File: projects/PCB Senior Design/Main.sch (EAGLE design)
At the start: 117 parts, among them IC1 74LVC2G34DBVR, J8 U.FL, J9 NANO_SIM, Q1 BSS138, Q2 2.5A/30V/105mΩ, U1 UBLOX_SAM_M8Q-0-10, U10 TCA9406DCU, U11 TXB0104, U13 LP2985-33DBVR, U2 32KB NRF51822, U3 MIC5225-3.3, U4 NCP1117ST50T3G, U6 SARA-R410M-2B, U7 MCP73831, U8 AP7361C-33FGE, U9 AP2112K-3.3, X1 POWERSUPPLY_DC21MMX, Y1 32.768kHz (535-9166-2-ND), Y2 CSTCE16M0V53-R0 16MHZ

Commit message: Made some connections
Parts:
- removed B2: ARDUINO_UNO_R3_SHIELDNOLABELS, SparkFun-Boards:ARDUINO_UNO_R3_SHIELDNOLABELS
- removed D9: PRTR5V0U2F, ublox:PRTR5V0U2F
- removed J15: (no value), SparkFun-Connectors:6_PIN_SERIAL_TARGETNO_SILK
- removed JP10: IOREF-SEL, SparkFun-Jumpers:JUMPER-SMT_3_NO_SILK
- removed JP6, JP9: JUMPER-SMT_2_NC_TRACE_SILK, SparkFun-Jumpers:JUMPER-SMT_2_NC_TRACE_SILK
- removed S3: PWR_ON, SparkFun-Switches:MOMENTARY-SWITCH-SPST-SMD-5.2-REDUNDANT
- removed S4: RESET, SparkFun-Switches:MOMENTARY-SWITCH-SPST-SMD-5.2-REDUNDANT
- removed S6: (no value), SparkFun-Switches:SWITCH-DPDT-SMD-AYZ0202
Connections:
- removed net +3V3: C33.2, U13.OUT
- removed net HARDRX-ARDUINO: B2.RX, S6.1
- removed net HARDTX-ARDUINO: B2.TX, S6.4
- removed net IOREF: B2.IOREF, C25.1, J15.VCC, JP10.2, U10.VCCB, U11.VCCB
- removed net N$10: B2.*D6, JP6.1
- removed net N$11: D9.1, J12.D-
- removed net N$13: D9.3, J12.D+
- removed net N$6: B2.*D5, JP9.1
- removed net RX-ARDUINO: J15.RXI, S6.2, U11.B2
- removed net SOFTRX-ARDUINO: B2.D8, S6.3
- removed net SOFTTX-ARDUINO: B2.*D9, S6.6
- removed net TX-ARDUINO: J15.TXO, S6.5, U11.B3
- new net RX-ARD: U11.B2, ZU4.(ICP)PB0
- new net TX-ARD: U11.B3, ZU4.(OC1)PB1
- net ARDUINO-3.3V: now also C33.2, U13.OUT; no longer B2.3.3V, JP10.3
- net ARDUINO-5V: now also C25.1, U10.VCCB, U11.VCCB; no longer B2.5V, JP10.1
- net D+: no longer D9.4
- net D-: no longer D9.6
- net GND: no longer B2.GND@0, B2.GND@1, B2.GND@2, D9.2, J15.GND, S3.1, S4.1
- net PWR_ON: now also ZU4.(T1)PD5; no longer JP9.2, S3.2
- net RESET_N: now also ZU4.(AIN0)PD6; no longer JP6.2, S4.2
- net V_USB: no longer D9.5
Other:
- note removed: "6-Pin Serial Port"
- note removed: "Arduino Pins"
- note removed: "Hardware Serial Port (D0 = RX, D1 = TX)"
- note removed: "If the Arduino does not supply IOREF, Use JP1 to set it to either 5V or 3.3V."
- note removed: "JP2 and JP3 can disconnect control lines from Arduino."
- note removed: "Software serial port (D8 = RX, D9 = TX)"
- note removed: "UART-Slect"
- moved on the sheet: C24, C25

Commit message: More cleaning up, serial to ATMega pt 1
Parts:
- removed C33: 1u, SmartPrj:C-EU0603-RND
- removed D7: Yellow, SparkFun-LED:LED-YELLOW0603
- removed D8: RED, SparkFun-LED:LED-RED0603
- removed FRAME3: FRAME-LETTER, SparkFun-Aesthetics:FRAME-LETTER
- removed J12: (no value), SparkFun-Connectors:USB_MICRO-B_HALF_PTH_MILL
- removed J13: (no value), SparkFun-Connectors:QWIIC_CONNECTORJS-1MM
- removed J14: (no value), SparkFun-Connectors:JST_2MM_MALESMD
- removed J16: (no value), SparkFun-Connectors:CONN_01PTH_NO_SILK_YES_STOP
- removed J17, J18: (no value), SparkFun-Connectors:CONN_021X02_NO_SILK
- removed J6, J7: (no value), SparkFun-Connectors:CONN_031X03_NO_SILK
- removed JP4, JP5: JUMPER-SMT_2_NC_TRACE_SILK, SparkFun-Jumpers:JUMPER-SMT_2_NC_TRACE_SILK
- removed PC1, PC2: 47u, rcl:CPOL-EUD
- removed R10: 1k, SparkFun-Resistors:1KOHM-0603-1/10W-1%
- removed R12: 1M, SmartPrj:R-EU_R0603
- removed R9: 2.0k, SparkFun-Resistors:2.0KOHM-0603-1/10W-5%
- removed S5: (no value), SparkFun-Switches:SWITCH-DPDT-SMD-AYZ0202
- removed TP_XT2: TP_SP, SmartPrj:TP_SP
- removed U10: TCA9406DCU, ublox:TCA9406DCU
- removed U11: TXB0104, SparkFun-IC-Comms:TXB0104PWR
- removed U13: LP2985-33DBVR, SmartPrj:LP2985-XXDBVR33
- removed X1: POWERSUPPLY_DC21MMX, SmartPrj:POWERSUPPLY_DC21MMX
- removed Y2: CSTCE16M0V53-R0 16MHZ, SmartPrj:RESONATORMU
- added C28: 22p, SmartPrj:C-EU0603-RND
- added C7: 4.7uF, SparkFun-Capacitors:4.7UF-0603-6.3V-(10%)
- added D12: RED, SparkFun-LED:LED-RED0603
- added D9: Yellow, SparkFun-LED:LED-YELLOW0603
- added F1: MF-MSMF050-2 500mA, rcl:L-EUL1812
- added J1: (no value), SparkFun-Connectors:USB_MICRO-B_HALF_PTH_MILL
- added J2: (no value), SparkFun-Connectors:JST_2MM_MALESMD
- added L3: BLM21, wuerth-elektronik:WE-CBF_0805
- added Q3: 2.5A/30V/105mΩ, SparkFun-DiscreteSemi:MOSFET_PCH-DMG2307L
- added Q4: 8MHz, special:XTAL
- added R15: 1k, SparkFun-Resistors:1KOHM-0603-1/10W-1%
- added RN2: 1K, resistor-dil:4R-NCAY16
- added RN3: 10K, resistor-dil:4R-NCAY16
- added RN4: 22R, resistor-dil:4R-NCAY16
- added U5: MCP73831, SparkFun-PowerIC:MCP73831
- added Z1, Z2: CG0603MLC-05E, varistor:VARISTORCN0603
- C21: value 4.7uF -> 0.1uF; device SparkFun-Capacitors:4.7UF-0603-6.3V-(10%) -> SparkFun-Capacitors:0.1UF-0603-25V-(+80/-20%)
- C22, C23: value 4.7uF -> 100n; device SparkFun-Capacitors:4.7UF-0603-6.3V-(10%) -> SmartPrj:C-EU0603-RND
- C24: value 0.1uF -> 1u; device SparkFun-Capacitors:0.1UF-0603-25V-(+80/-20%) -> SmartPrj:C-EU0603-RND
- C25: value 0.1uF -> 22p; device SparkFun-Capacitors:0.1UF-0603-25V-(+80/-20%) -> SmartPrj:C-EU0603-RND
- C26, C27: value 1.0uF -> 4.7uF; device SparkFun-Capacitors:1.0UF-0603-16V-10% -> SparkFun-Capacitors:4.7UF-0603-6.3V-(10%)
- C6: value 100n -> 0.1uF; device SmartPrj:C-EU0603-RND -> SparkFun-Capacitors:0.1UF-0603-25V-(+80/-20%)
- D1: value M7 -> 1A/23V/620mV; device diode:DIODE-SMB -> SparkFun-DiscreteSemi:DIODE-SCHOTTKY-BAT20J
- D5: value 1A/23V/620mV -> CD1206-S01575; device SparkFun-DiscreteSemi:DIODE-SCHOTTKY-BAT20J -> diode:DIODE-MINIMELF
- Q2: value 2.5A/30V/105mΩ -> 8MHz; device SparkFun-DiscreteSemi:MOSFET_PCH-DMG2307L -> special:XTAL
- R1: value 470 -> 10k; device SparkFun-Resistors:470OHM-0603-1/10W-1% -> SparkFun-Resistors:10KOHM-0603-1/10W-1%
- R11: value 47k -> 2.0k; device SparkFun-Resistors:47KOHM-0603-1/10W-1% -> SparkFun-Resistors:2.0KOHM-0603-1/10W-5%
- R2: value 470 -> 1k; device SparkFun-Resistors:470OHM-0603-1/10W-1% -> SparkFun-Resistors:1KOHM-0603-1/10W-1%
- R6: value 10k -> 1M; device SparkFun-Resistors:10KOHM-0603-1/10W-1% -> SmartPrj:R-EU_R0603
- R7: value 1k -> 1M; device SparkFun-Resistors:1KOHM-0603-1/10W-1% -> SmartPrj:R-EU_R0603
- U4: value NCP1117ST50T3G -> TCA9406DCU; device linear:MC33269ST-3.3T3 -> ublox:TCA9406DCU
- U7: value MCP73831 -> TXB0104; device SparkFun-PowerIC:MCP73831 -> SparkFun-IC-Comms:TXB0104PWR
- U8: value AP7361C-33FGE -> ATMEGA16U2-MU(R); device ublox:AP7361C-33FGE -> SmartPrj:ATMEGA16U2-MU
- U9: value AP2112K-3.3 -> AP7361C-33FGE; device SparkFun-IC-Power:V_REG_AP2112K-3.3V -> ublox:AP7361C-33FGE
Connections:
- net ANT_DET renamed N$2
- removed net !RESET: U1.!RST
- removed net !SAFE: U1.!SAFEBOOT
- removed net AD4/SDA: ZU4.(ADC4)PC4
- removed net AD5/SCL: ZU4.(ADC5)PC5
- removed net ARDUINO-3.3V: C33.2, U13.OUT
- removed net ARDUINO-5V: C25.1, S5.2, S5.5, U10.VCCB, U11.VCCB
- removed net CTS: J7.3, U6.CTS
- removed net DCD: J6.2, U6.DCD
- removed net DSR: J6.1, U6.DSR
- removed net GPIO2: R11.2, U6.GPIO2, U9.EN
- removed net GPIO3-CELL: U11.A1, U6.GPIO3
- removed net GPIO3-QWIIC: J16.1, U11.B1
- removed net GPS-3.3V: C27.1, J13.2, U9.OUT
- removed net INT: U1.INT
- removed net N$2 (its old number): D7.C, R7.2
- removed net N$3: R7.1, U7.STAT
- removed net N$4: R9.2, U7.PROG
- removed net N$5: D8.A, R10.1
- removed net NETWORK_LED: U6.GPIO1
- removed net PPS: U1.TPULSE
- removed net PWRIN: D1.A, X1.2
- removed net RI: J7.1, U6.RI
- removed net RTS: J6.3, JP4.2, U6.RTS
- removed net RXI: R2.2
- removed net RXLV: R2.1, U1.RX
- removed net SCL: R14.2, R3.1
- removed net SCL-QWIIC: J13.4, J17.2, U10.SCL_B
- removed net SDA: R13.2, R4.1
- removed net SDA-QWIIC: J13.3, J17.1, U10.SDA_B
- removed net TXLV: R1.1, U1.TX
- removed net TXO: R1.2
- removed net VUSB_DET: U6.VUSB_DET
- new net GPIO3-CELL1: U7.A1
- new net GPIO3-QWIIC1: U7.B1
- new net M8RXD: U8.(TXD1/INT3)PD3
- new net M8TXD: U8.(RXD1/AIN1/INT2)PD2
- new net N$1: D9.C, R2.2
- new net N$10: R11.2, U5.PROG
- new net N$11: D12.A, R15.1
- new net N$6: R2.1, U5.STAT
- new net RD+: RN4D.1, U8.D+
- new net RD-: RN4A.1, U8.D-
- new net RESET1: C23.2
- new net RESET2: D5.A, RN3C.2, U8.RESET(PC1/DW)
- new net SCL-GPS: R14.2, R3.1, U4.SCL_B
- new net SDA-GPS: R13.2, R4.1, U4.SDA_B
- new net TP_VUCAP: C24.1, U8.UCAP
- new net USBVCC: F1.1, U8.UVCC
- new net XT1: C25.1, Q4.1, R6.1, U8.XTAL1
- new net XT2: C28.1, Q4.2, R6.2, U8.XTAL2(PC0)
- net +5V: now also C22.1, D5.C, RN3C.1, U8.AVCC, U8.VCC; no longer C31.2, C6.2, D3.C, ICSP.2, L4.1, PC2.+, RN1D.2, U13.IN, U13.ON/!OFF, U4.OUT, U4.OUT@1, ZU4.VCC
- net 1.8V: now also C6.1, U4.OE, U4.VCCA, U7.OE, U7.VCCA; no longer C24.1, U10.OE, U10.VCCA, U11.OE, U11.VCCA
- net 3.3V: now also C21.1, C27.1, C31.2, D3.C, ICSP.2, L4.1, R15.2, RN1D.2, U4.VCCB, U7.VCCB, U9.OUT, ZU4.VCC; no longer C23.1, C26.1, R10.2, U8.OUT, U9.IN
- net D+: now also J1.D+, RN4D.2, Z1.1; no longer U6.USB_D+
- net D-: now also J1.D-, RN4A.2, Z2.1; no longer U6.USB_D-
- net DTR: now also C23.1, RN2D.1, U8.(CTS/HWB/AIN6/TO/INT7)PD7; no longer J7.2, JP5.2, U6.DTR
- net GND: now also C28.2, C6.2, C7.2, D12.C, J1.GND, J2.-, L3.1, R1.1, RN2D.2, U4.GND, U5.VSS, U6.DTR, U6.RTS, U7.GND, U8.PAD, U8.UGND; no longer C23.2, C33.1, C6.1, D8.C, J12.GND, J13.1, J14.-, J18.1, JP4.1, JP5.1, PC1.-, PC2.-, R6.1, R9.1, U10.GND, U11.GND, U13.GND, U4.GND/ADJ, U7.VSS, X1.1, X1.3, Y2.2
- net RX-ARD: now also U7.B2; no longer U11.B2
- net RX-CELL: now also U7.A3; no longer U11.A3
- net SCL-CELL: now also U4.SCL_A; no longer U10.SCL_A
- net SDA-CELL: now also U4.SDA_A; no longer U10.SDA_A
- net SHIELD: now also J1.SHIELD, L3.2, Z1.2, Z2.2; no longer J12.SHIELD
- net TX-ARD: now also U7.B3; no longer U11.B3
- net TX-CELL: now also U7.A2; no longer U11.A2
- net VIN: now also C26.1, Q3.S, U9.EN, U9.IN; no longer C22.1, D5.C, PC1.+, Q2.S, S5.1, S5.4, U4.IN, U8.EN, U8.IN
- net V_BATT: now also C7.1, J2.+, Q3.D, U5.VBAT; no longer C21.1, J14.+, J18.2, Q2.D, U7.VBAT
- net V_USB: now also D1.A, D9.A, F1.2, J1.VBUS, Q3.G, R1.2, U5.VIN; no longer D5.A, D7.A, J12.VBUS, Q2.G, R6.2, S5.3, S5.6, U7.VIN
- net XTAL1: now also Q2.1, R7.1; no longer R12.1, Y2.3
- net XTAL2: now also Q2.2, R7.2; no longer R12.2, TP_XT2.TESTP, Y2.1
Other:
- note added: "Arduino(TM) UNO Rev3"
- note added: "GPS Comms"
- note added: "Note: Needs caps"
- note added: "Note: Original schematic does not have these level shifted down from Arduino."
- note added: "USB boot En"
- note removed: "Battery Charger / Voltage Regulator"
- note removed: "GPIO2 controls power to the GPS module by enabling/disabling the 3.3V LDO."
- note removed: "GPIO3 is an optional interrupt output from the GPS module to the SARA module."
- note removed: "JP4 and JP5 short RTS and DTR to GND. This is the recommended configuration for a UART with NO FLOW CONTROL."
- note removed: "Note: UART RX/TX pin names on SARA module are w/ respect to DTE (Arduino)."
- note removed: "Power Arduino from shield (Arduino 5V pin supplies power to shield.)"
- note removed: "Power Select"
- note removed: "Power shield from Arduino (Shield USB or battery supplies power to Arduino)"
- note removed: "UART Handshake Signals"
- note removed: "u-blox GPS I2C Port"

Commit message: stuff
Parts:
- removed C36: 100n, SmartPrj:C-EU0603-RND
- removed C4: 10uF, microbuilder:CAP_CERAMIC0805-NOOUTLINE
- removed C5: 10uF, microbuilder:CAP_CERAMIC0805_10MGAP
- removed D10: BLUE, microbuilder:LED0805_NOOUTLINE
- removed D3, D5: CD1206-S01575, diode:DIODE-MINIMELF
- removed D4: RED, microbuilder:LED0805_NOOUTLINE
- removed IC1: 74LVC2G34DBVR, microbuilder:74LVC2G34DBVR
- removed L4: 10uH, Induttanze:0715_CV201210-100K
- removed Q1: BSS138, microbuilder:MOSFET-NWIDE
- removed R16, R17: 2K, microbuilder:RESISTOR_0805MP
- removed R18, R19: 100K, microbuilder:RESISTOR0805_NOOUTLINE
- removed RN2: 1K, resistor-dil:4R-NCAY16
- removed TP1: SWCLK, microbuilder:TESTPOINT1.5X2.0MM_NOCREAM
- removed TP2: SWDIO, microbuilder:TESTPOINT1.5X2.0MM_NOCREAM
- removed TP3: FCTRST, microbuilder:TESTPOINT1.5X2.0MM_NOCREAM
- removed U3: MIC5225-3.3, microbuilder:VREG_SOT23-5
- removed VTREF: THREEV, microbuilder:TESTPOINT1.5X2.0MM_NOCREAM
- added C29, C30: 22p, SmartPrj:C-EU0603-RND
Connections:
- net CS_3V renamed CS-BT
- net IRQ_3V renamed IRQ-BT
- net MISO_3V renamed MISO-BT
- removed net +5V: C22.1, D5.C, RN3C.1, U8.AVCC, U8.VCC
- removed net AREF: ZU4.AREF
- removed net AVCC: C36.2, L4.2, ZU4.AVCC
- removed net MOSI_3V: IC1.2Y, U2.P0.23
- removed net MOSI_5V: IC1.2A
- removed net N$14: ZU4.(RXD)PD0
- removed net N$15: ZU4.(TXD)PD1
- removed net N$19: D4.A, R16.2
- removed net N$20: D10.A, R17.2
- removed net RESET: D3.A, ICSP.5, RESET.3, RESET.4, RN1D.1, ZU4.RESET
- removed net SCK_3V: IC1.1Y, U2.P0.21
- removed net SCK_5V: IC1.1A
- removed net SWDIO/RST_5V: Q1.D, R18.2
- new net MOSI-BT: U2.P0.23
- new net SCK-BT: U2.P0.21
- net 3.3V: now also C22.1, RN3C.1, U8.AVCC, U8.VCC, ZU4.AVCC; no longer C5.1, D3.C, IC1.VCC, L4.1, Q1.G, R19.1, U3.OUT, VTREF.P$1
- net CONNECTED: no longer R17.1
- net DTR: no longer RN2D.1
- net FACTORYRST: no longer TP3.P$1
- net GND: now also C29.2, C30.2; no longer C36.1, C4.2, C5.2, D10.C, D4.C, IC1.GND, RN2D.2, U3.GND
- net M8RXD: now also ZU4.(RXD)PD0
- net M8TXD: now also ZU4.(TXD)PD1
- net MODE: no longer R16.1
- net RESET1: now also ICSP.5, RESET.3, RESET.4, RN1D.1, ZU4.RESET
- net RESET2: no longer D5.A
- net SWCLK: no longer TP1.P$1
- net SWDIO/RST_3V: no longer Q1.S, R19.2, TP2.P$1
- net VIN: no longer C4.1, R18.1, U3.EN, U3.IN
- net XTAL1: now also C30.1
- net XTAL2: now also C29.1
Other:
- note added: "ATMega must be ordered with bootloader already installed."
- note removed: "Arduino(TM) UNO Rev3"
- note removed: "Note: Needs caps"
- note removed: "REV- F CHANGES: Removed Factory Reset (now uses DFU) Removed DFU button (pin only) Removed extra test points and SWD connector"
- note removed: "USB boot En"
- moved on the sheet: C22, C23, C24, C25, C28, C3, C31, D11, F1, ICSP, L3, Q2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

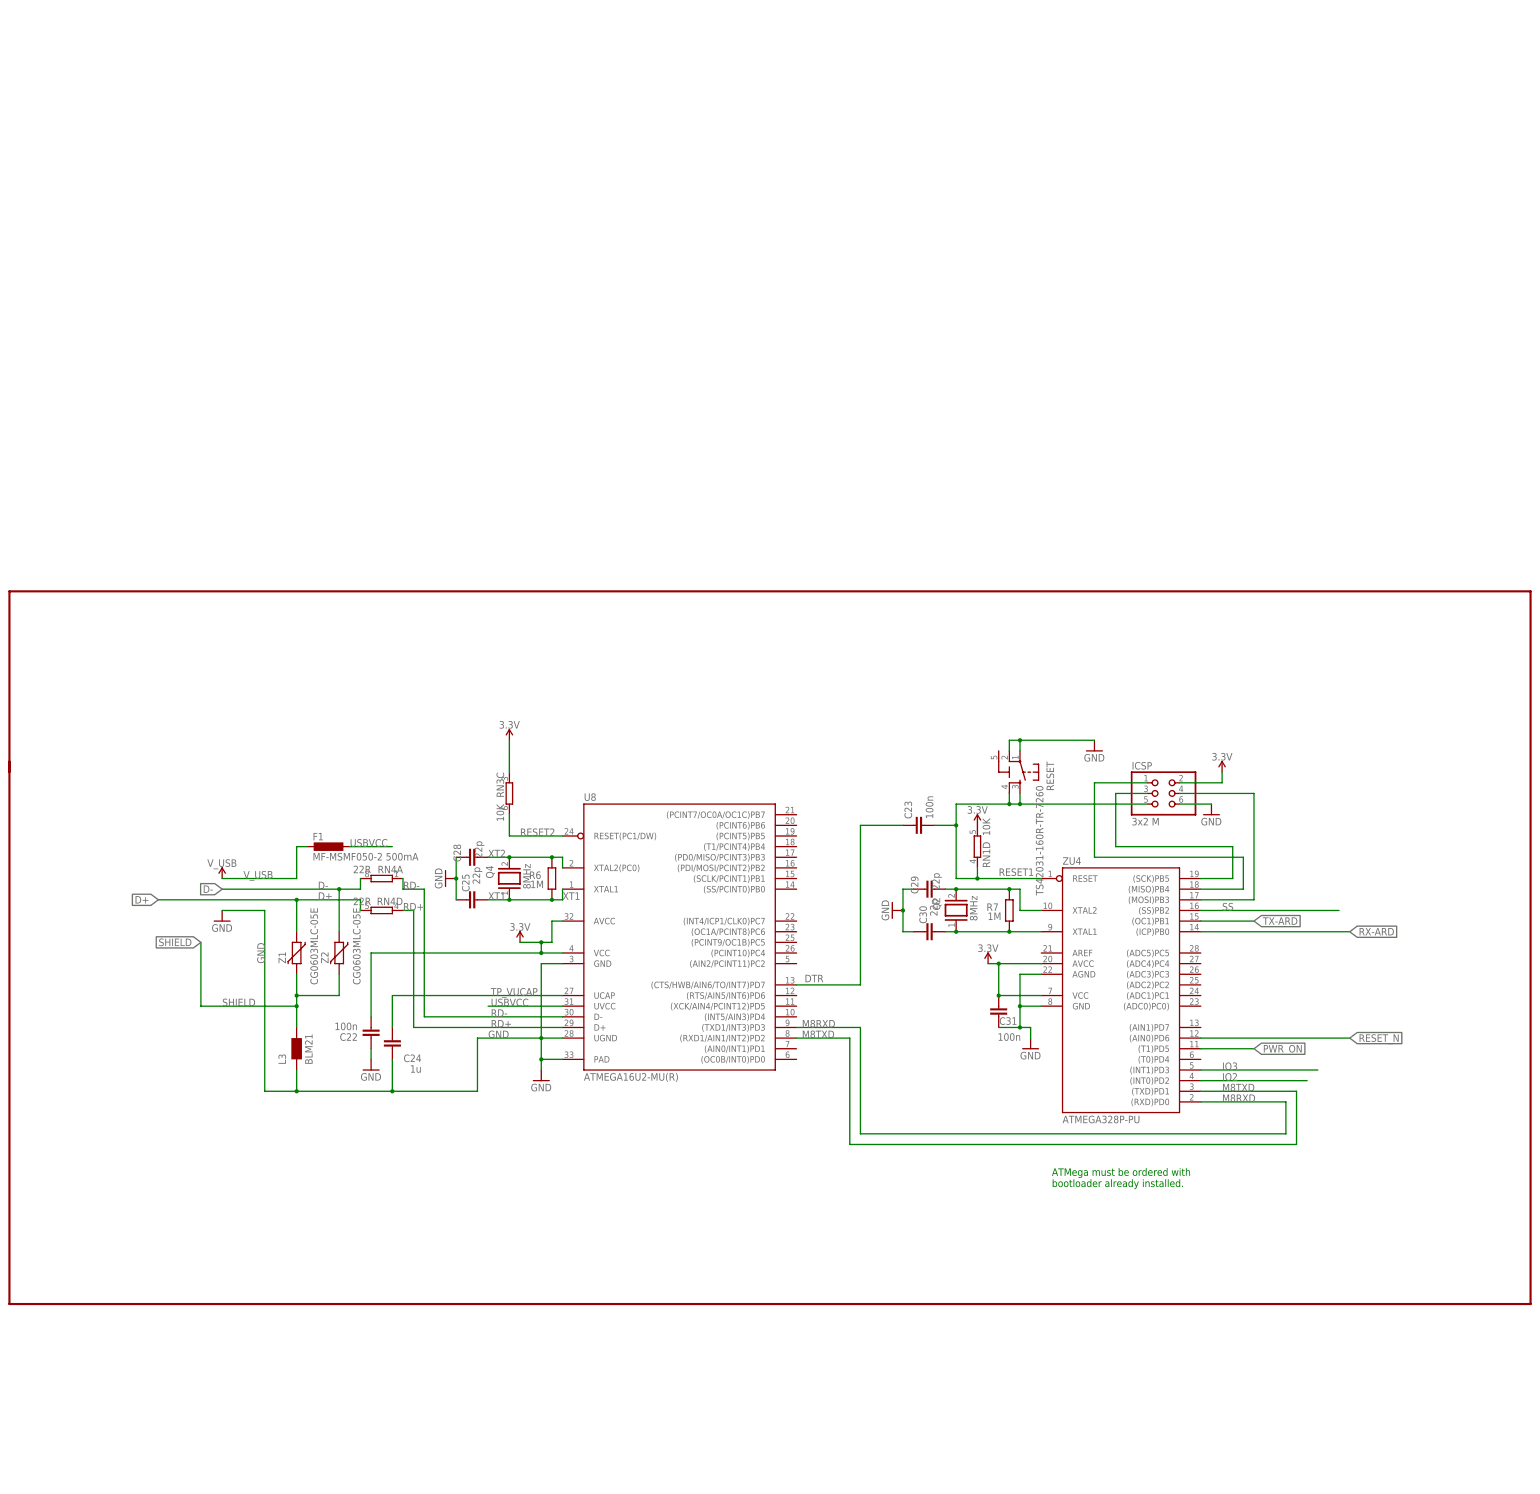
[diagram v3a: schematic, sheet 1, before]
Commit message: Back to ISP programming. Cleaned up BT module
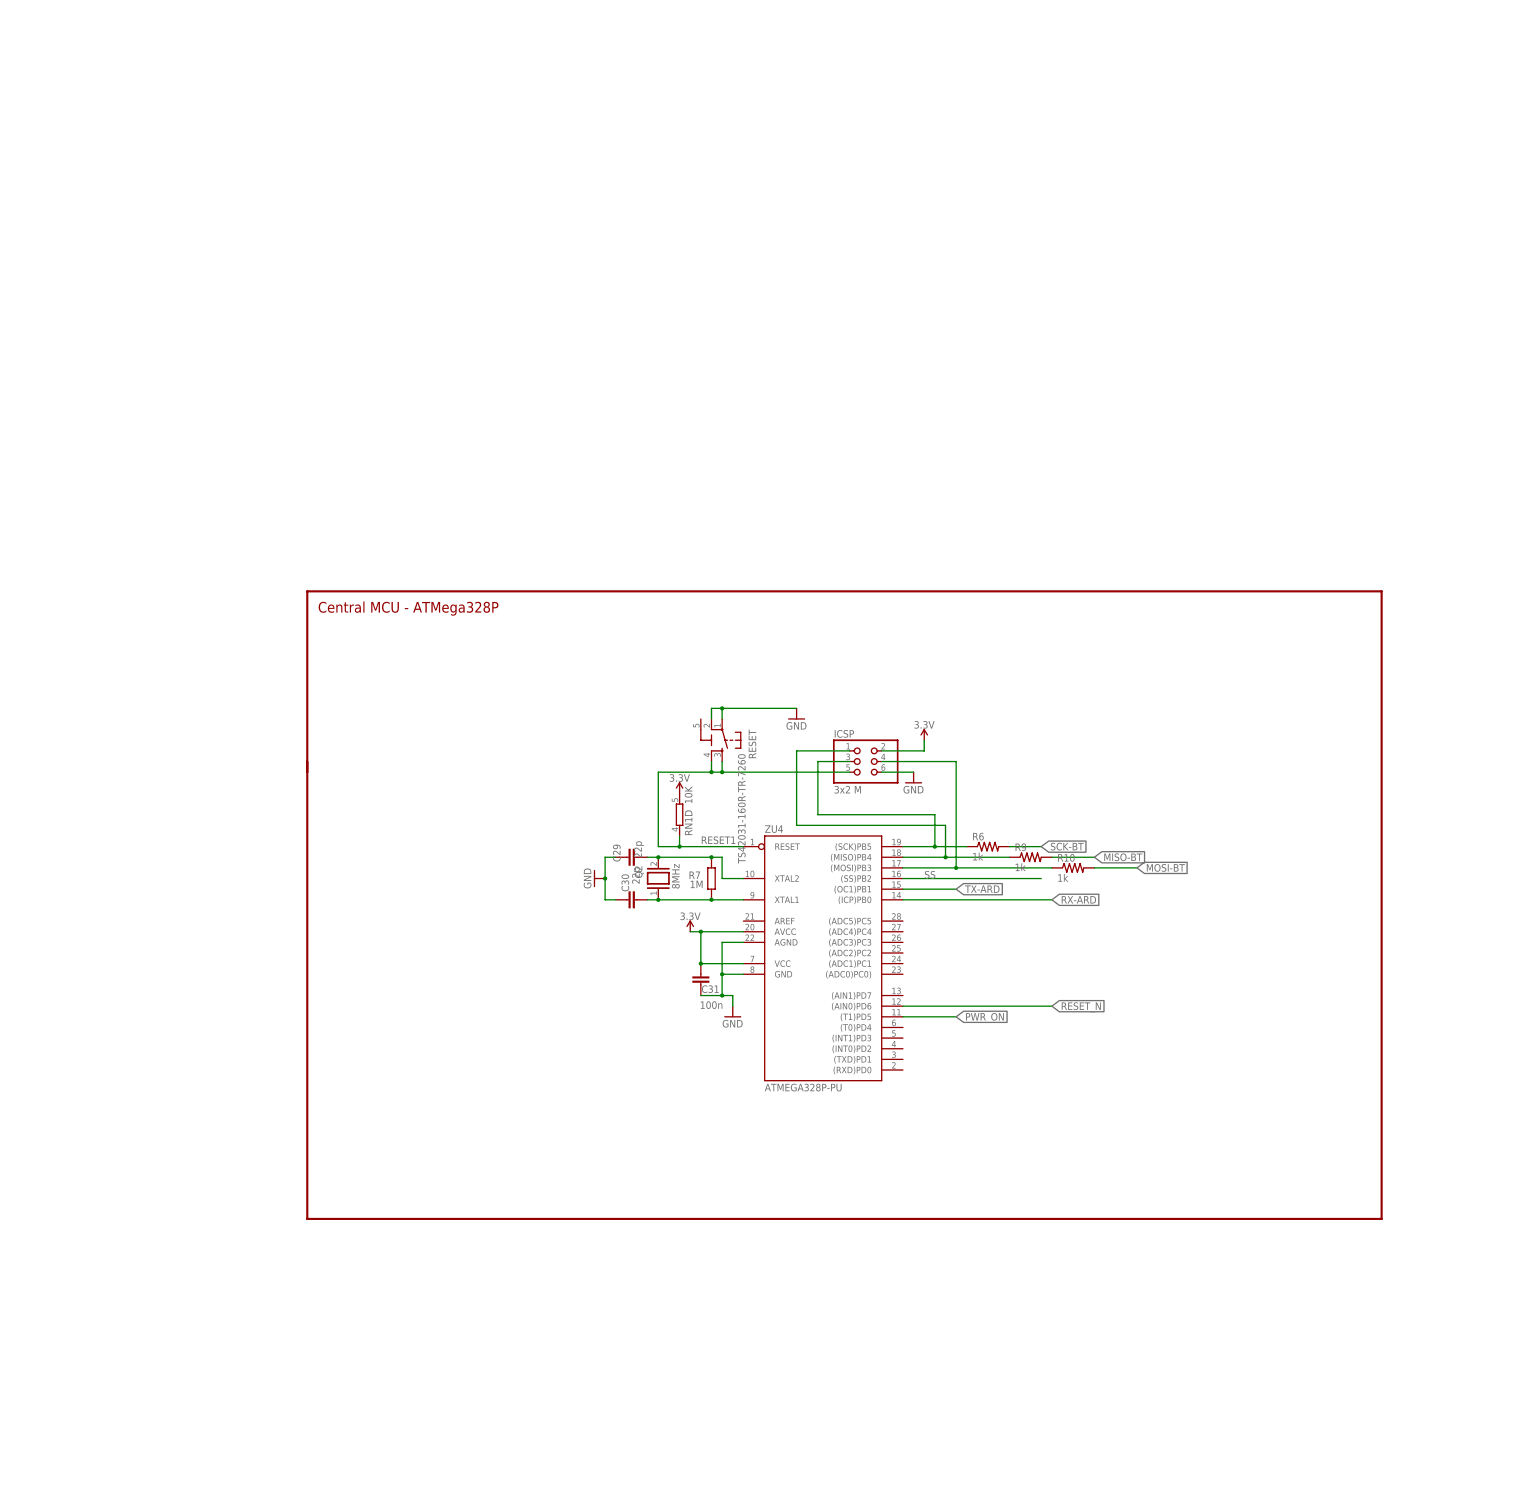
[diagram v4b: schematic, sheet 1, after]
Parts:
- removed C22, C23: 100n, SmartPrj:C-EU0603-RND
- removed C24: 1u, SmartPrj:C-EU0603-RND
- removed C25, C28: 22p, SmartPrj:C-EU0603-RND
- removed F1: MF-MSMF050-2 500mA, rcl:L-EUL1812
- removed L3: BLM21, wuerth-elektronik:WE-CBF_0805
- removed Q4: 8MHz, special:XTAL
- removed RN3: 10K, resistor-dil:4R-NCAY16
- removed RN4: 22R, resistor-dil:4R-NCAY16
- removed U8: ATMEGA16U2-MU(R), SmartPrj:ATMEGA16U2-MU
- removed Z1, Z2: CG0603MLC-05E, varistor:VARISTORCN0603
- added R10, R9: 1k, rcl:R-US_R0201
- R6: value 1M -> 1k; device SmartPrj:R-EU_R0603 -> rcl:R-US_R0201
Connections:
- removed net DTR: C23.1, U8.(CTS/HWB/AIN6/TO/INT7)PD7
- removed net IO2: ZU4.(INT0)PD2
- removed net IO3: ZU4.(INT1)PD3
- removed net M8RXD: U8.(TXD1/INT3)PD3, ZU4.(RXD)PD0
- removed net M8TXD: U8.(RXD1/AIN1/INT2)PD2, ZU4.(TXD)PD1
- removed net RD+: RN4D.1, U8.D+
- removed net RD-: RN4A.1, U8.D-
- removed net RESET2: RN3C.2, U8.RESET(PC1/DW)
- removed net TP_VUCAP: C24.1, U8.UCAP
- removed net USBVCC: F1.1, U8.UVCC
- removed net XT1: C25.1, Q4.1, R6.1, U8.XTAL1
- removed net XT2: C28.1, Q4.2, R6.2, U8.XTAL2(PC0)
- net 3.3V: no longer C22.1, RN3C.1, U8.AVCC, U8.VCC
- net D+: no longer RN4D.2, Z1.1
- net D-: no longer RN4A.2, Z2.1
- net GND: no longer C22.2, C24.2, C25.2, C28.2, L3.1, U8.GND, U8.PAD, U8.UGND
- net MISO: now also R9.1
- net MISO-BT: now also R9.2
- net MOSI: now also R10.1
- net MOSI-BT: now also R10.2
- net RESET1: no longer C23.2
- net SCK: now also R6.1
- net SCK-BT: now also R6.2
- net SHIELD: no longer L3.2, Z1.2, Z2.2
- net V_USB: no longer F1.2
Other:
- note added: "Central MCU - ATMega328P"
- note added: "Power Management"
- note added: "SARA-R4 Cellular Module"
- note added: "Ublox SAM-M8Q GPS Module"
- note added: "nRF51822 Bluetooth Module"
- note removed: "ATMega must be ordered with bootloader already installed."
- note removed: "SARA-R4 Module"
- note removed: "Ublox SAM-M8Q"
- moved on the sheet: BT1, C1, C2, C29, C30, C31, D2, ICSP, Q2, R13, R14, R3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
